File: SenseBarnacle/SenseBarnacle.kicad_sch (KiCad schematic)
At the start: 109 parts, among them J1 USB_B_Mini, J2 Debug, J3 Power, J5 I2C_OLED_Display, J6 Conn_02x35_JumperluxCardEdge, J7 Conn_02x35_JumperluxCardEdge, SW1 USB BOOT, U1 LM324, U13 CH446X, U14 CH446X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

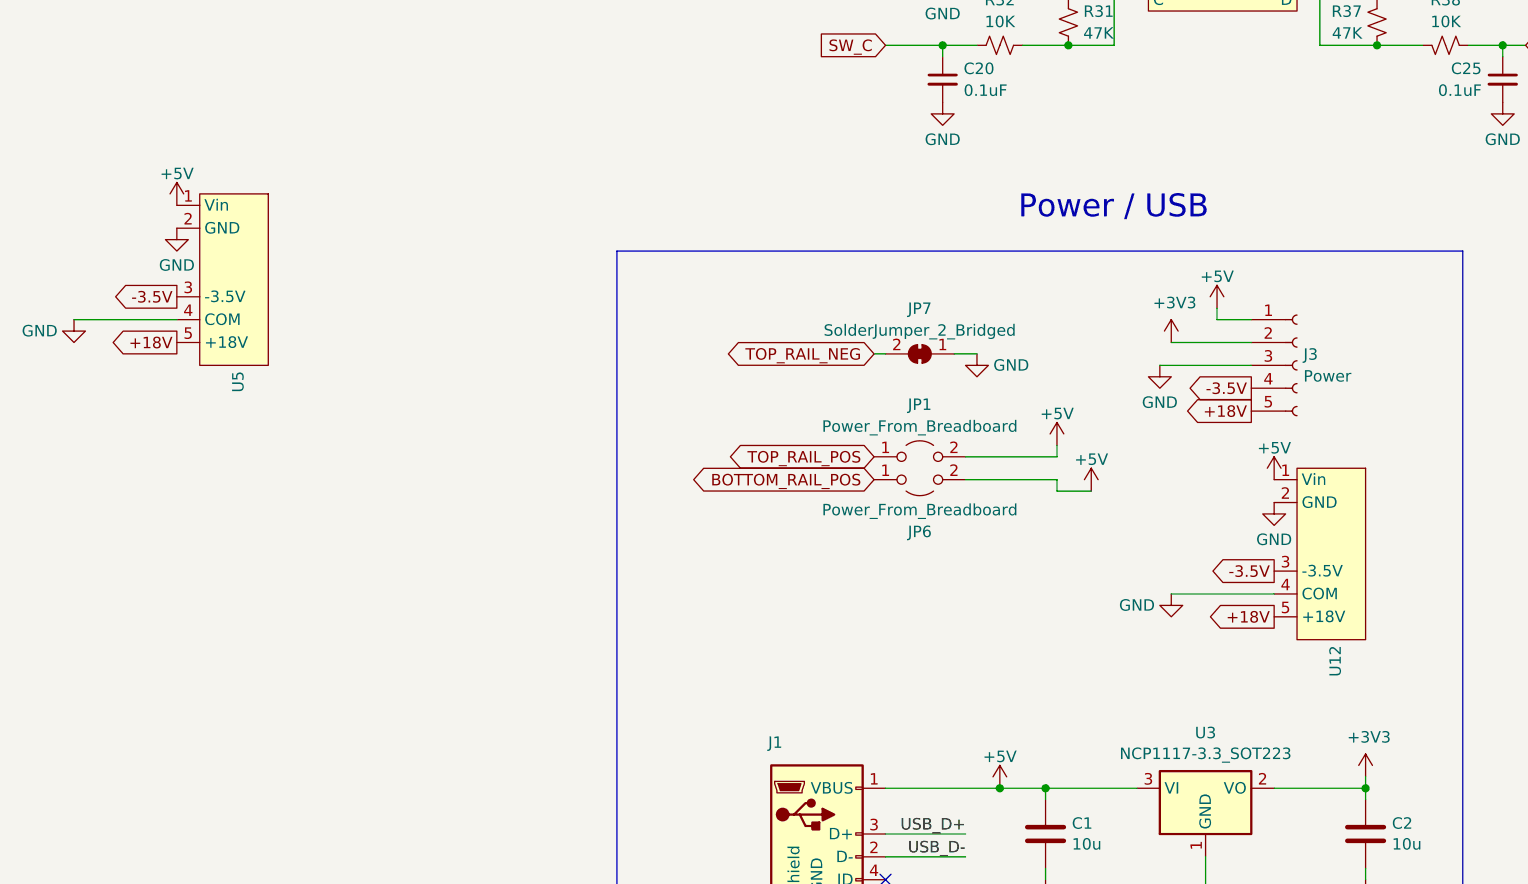
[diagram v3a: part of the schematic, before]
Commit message: Added silkscreen
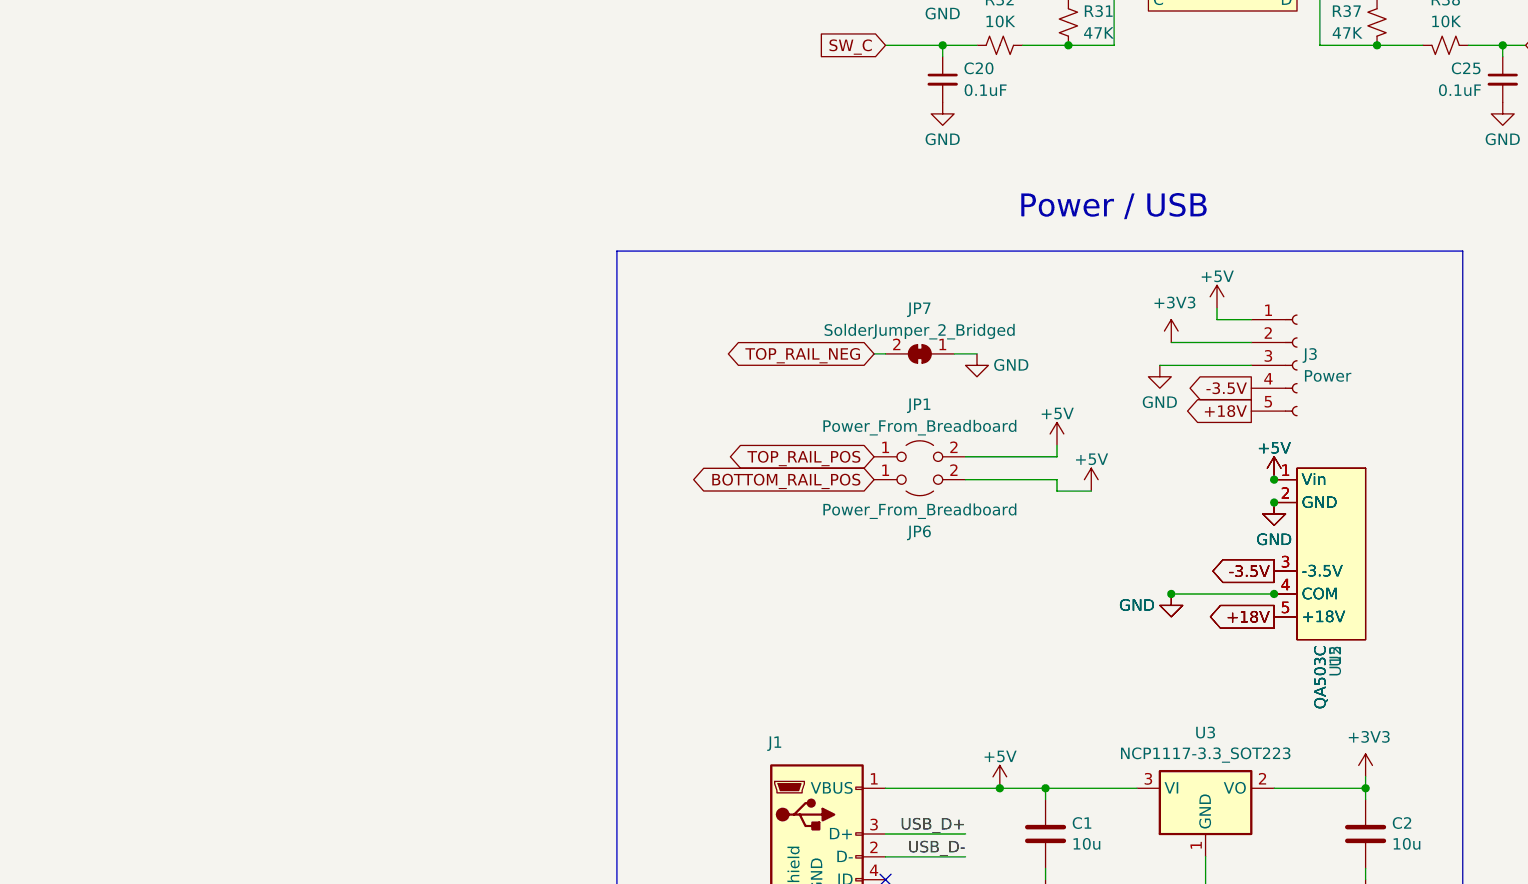
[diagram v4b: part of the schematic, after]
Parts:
- U12, U5: value ~ -> QA503C
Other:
- moved on the sheet: U5
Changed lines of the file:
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@@
 	)
 	(junction
+		(at 91.44 222.25)
+		(diameter 0)
+		(color 0 0 0 0)
+	)
+	(junction
 		(at 438.15 58.42)
 		(diameter 0)
@@
 	)
 	(junction
+		(at 91.44 212.09)
+		(diameter 0)
+		(color 0 0 0 0)
+	)
+	(junction
 		(at 68.58 161.29)
 		(diameter 0)
@@
 	)
 	(junction
+		(at 91.44 209.55)
+		(diameter 0)
+		(color 0 0 0 0)
+	)
+	(junction
 		(at 182.88 262.89)
 		(diameter 0)
@@
 	)
 	(junction
+		(at 80.01 222.25)
+		(diameter 0)
+		(color 0 0 0 0)
+	)
+	(junction
 		(at 163.83 247.015)
 		(diameter 0)
@@
 	(wire
 		(pts
-			(xy -41.91 191.77) (xy -30.48 191.77)
-		)
-		(stroke
-			(width 0)
-			(type default)
-		)
-	)
-	(wire
-		(pts
 			(xy 190.5 262.89) (xy 193.04 262.89)
 		)
@@
 	(global_label "+18V"
 		(shape output)
-		(at -30.48 194.31 180)
+		(at 91.44 224.79 180)
 		(fields_autoplaced yes)
 		(effects
@@
 		)
 		(property "Intersheetrefs" "${INTERSHEET_REFS}"
-			(at -38.5452 194.31 0)
+			(at 83.3748 224.79 0)
 			(effects
 				(font
@@
 	(global_label "-3.5V"
 		(shape output)
-		(at -30.48 189.23 180)
+		(at 91.44 219.71 180)
 		(fields_autoplaced yes)
 		(effects
@@
 		)
 		(property "Intersheetrefs" "${INTERSHEET_REFS}"
-			(at -39.15 189.23 0)
+			(at 82.77 219.71 0)
 			(effects
 				(font
@@
 	(symbol
 		(lib_id "JumperlessSymbols:QA053C-1803R3")
-		(at -27.94 184.15 270)
+		(at 93.98 214.63 270)
 		(unit 1)
 		(exclude_from_sim no)
@@
 		(fields_autoplaced yes)
 		(property "Reference" "U5"
-			(at -23.6608 197.485 0)
+			(at 98.2592 227.965 0)
 			(effects
 				(font
@@
 			)
 		)
-		(property "Value" "~"
-			(at -25.3422 197.485 0)
+		(property "Value" "QA503C"
+			(at 96.5778 227.965 0)
 			(effects
 				(font
@@
 		)
 		(property "Footprint" "JumperlessFootprints:QA503C"
-			(at -27.94 185.42 0)
+			(at 93.98 215.9 0)
 			(effects
 				(font
@@
 		)
 		(property "Datasheet" ""
-			(at -27.94 185.42 0)
+			(at 93.98 215.9 0)
 			(effects
 				(font
@@
 		)
 		(property "Description" ""
-			(at -27.94 185.42 0)
+			(at 93.98 215.9 0)
 			(effects
 				(font
@@
 		(lib_name "GND_40")
 		(lib_id "power:GND")
-		(at -41.91 191.77 0)
+		(at 80.01 222.25 0)
 		(unit 1)
 		(exclude_from_sim no)
@@
 		(dnp no)
 		(property "Reference" "#PWR079"
-			(at -41.91 198.12 0)
+			(at 80.01 228.6 0)
 			(effects
 				(font
@@
 		)
 		(property "Value" "GND"
-			(at -45.72 193.04 0)
+			(at 76.2 223.52 0)
 			(effects
 				(font
@@
 		)
 		(property "Footprint" ""
-			(at -41.91 191.77 0)
+			(at 80.01 222.25 0)
 			(effects
 				(font
@@
 		)
 		(property "Datasheet" ""
-			(at -41.91 191.77 0)
+			(at 80.01 222.25 0)
 			(effects
 				(font
@@
 		)
 		(property "Description" ""
-			(at -41.91 191.77 0)
+			(at 80.01 222.25 0)
 			(effects
 				(font
@@
 			)
 		)
-		(property "Value" "~"
+		(property "Value" "QA503C"
 			(at 96.5778 227.965 0)
 			(effects
@@
 	(symbol
 		(lib_id "power:+5V")
-		(at -30.48 179.07 0)
+		(at 91.44 209.55 0)
 		(unit 1)
 		(exclude_from_sim no)
@@
 		(fields_autoplaced yes)
 		(property "Reference" "#PWR035"
-			(at -30.48 182.88 0)
+			(at 91.44 213.36 0)
 			(effects
 				(font
@@
 		)
 		(property "Value" "+5V"
-			(at -30.48 175.5681 0)
+			(at 91.44 206.0481 0)
 			(effects
 				(font
@@
 		)
 		(property "Footprint" ""
-			(at -30.48 179.07 0)
+			(at 91.44 209.55 0)
 			(effects
 				(font
@@
 		)
 		(property "Datasheet" ""
-			(at -30.48 179.07 0)
+			(at 91.44 209.55 0)
 			(effects
 				(font
@@
 		)
 		(property "Description" ""
-			(at -30.48 179.07 0)
+			(at 91.44 209.55 0)
 			(effects
 				(font
@@
 	(symbol
 		(lib_id "power:GND")
-		(at -30.48 181.61 0)
+		(at 91.44 212.09 0)
 		(unit 1)
 		(exclude_from_sim no)
@@
 		(fields_autoplaced yes)
 		(property "Reference" "#PWR038"
-			(at -30.48 187.96 0)
+			(at 91.44 218.44 0)
 			(effects
 				(font
@@
 		)
 		(property "Value" "GND"
-			(at -30.48 185.7431 0)
+			(at 91.44 216.2231 0)
 			(effects
 				(font
@@
 		)
 		(property "Footprint" ""
-			(at -30.48 181.61 0)
+			(at 91.44 212.09 0)
 			(effects
 				(font
@@
 		)
 		(property "Datasheet" ""
-			(at -30.48 181.61 0)
+			(at 91.44 212.09 0)
 			(effects
 				(font
@@
 		)
 		(property "Description" "Power symbol creates a global label with name \"GND\" , ground"
-			(at -30.48 181.61 0)
+			(at 91.44 212.09 0)
 			(effects
 				(font
